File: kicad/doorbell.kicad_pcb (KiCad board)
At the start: 4 copper layers, 52.7 x 58.2 mm, 67 parts, among them J1 USB-C (USB4105), J2 WF26 (6-way screw), K1 G6K-2F-Y 4.5V, K2 G6K-2F-Y 4.5V, K3 G6K-2F-Y 4.5V, Q1 2N7002, Q2 2N7002, Q3 2N7002, SW1 BOOT, SW2 EN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

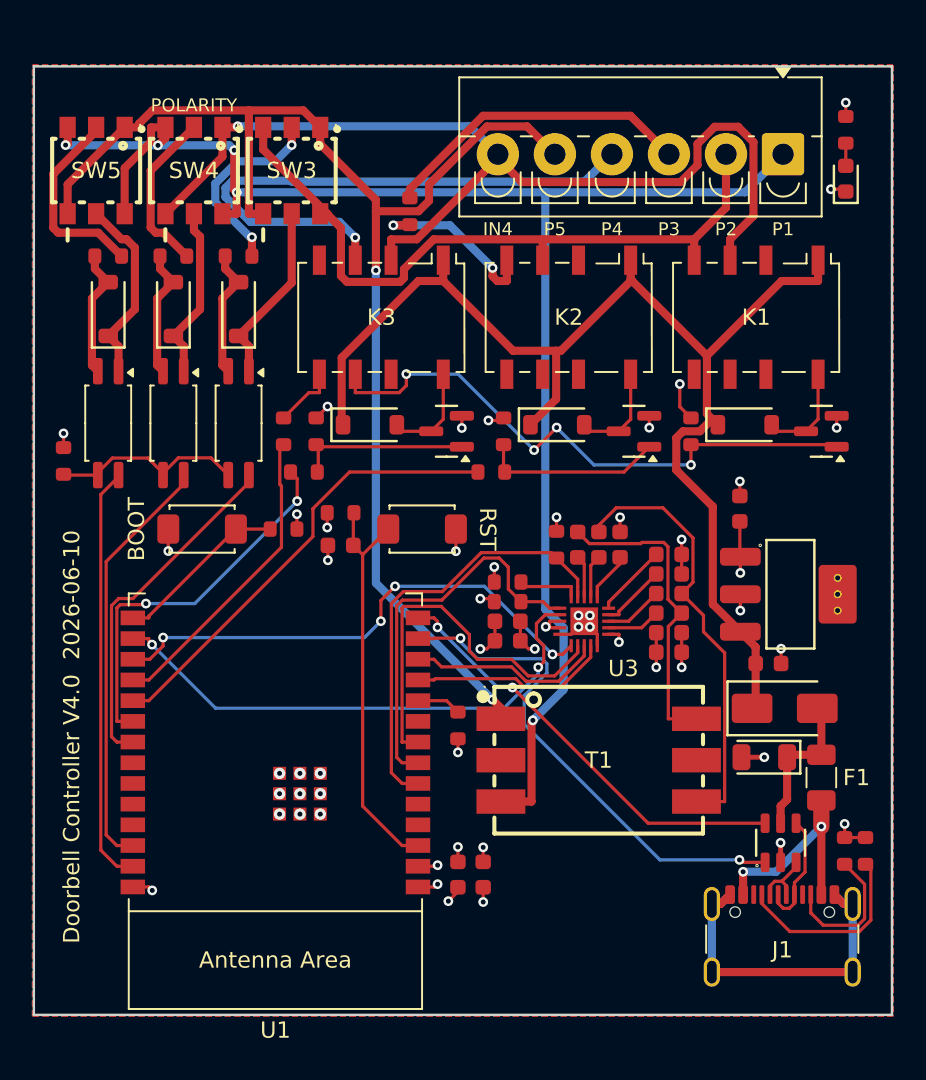
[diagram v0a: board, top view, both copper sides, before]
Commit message: Hand-route GPIO escape bundle; swap GATE pins for crossing-free fan-out
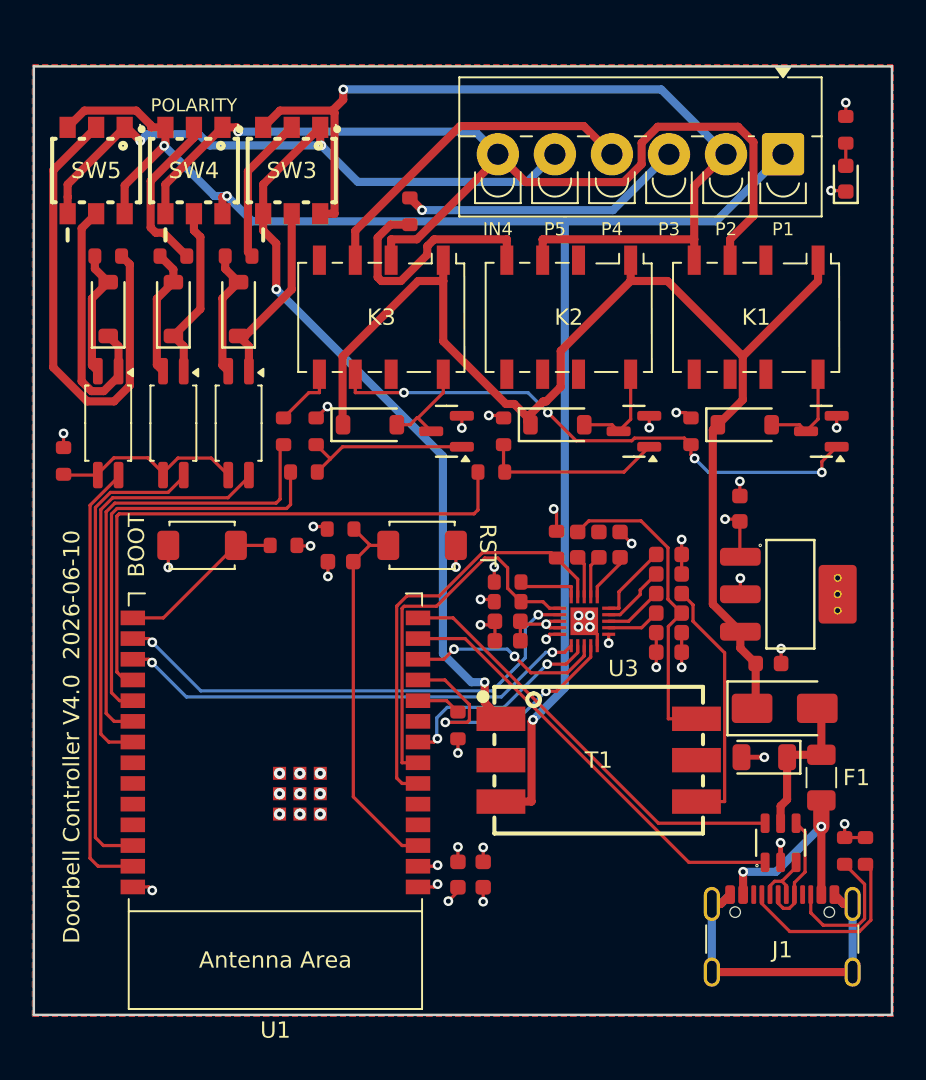
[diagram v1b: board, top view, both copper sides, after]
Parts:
- moved C5 1.00 mm to (17.0, 42.0)
- moved R10 1.00 mm to (17.0, 40.0)
- moved R11 1.00 mm to (13.5, 41.0)
- moved SW1 1.00 mm to (8.50, 41.0)
- moved SW2 1.00 mm to (22.0, 41.0)
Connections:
- U1 pad 18: GATE1_DRV -> GATE2_DRV
- U1 pad 19: GATE2_DRV -> GATE3_DRV
- U1 pad 20: GATE3_DRV -> GATE1_DRV
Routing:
- net OC3_RET: track 12.2 -> 29.9 mm
- net P4: track 35.6 -> 20.9 mm, vias 1 -> 0
- net P2: track 43.4 -> 56.5 mm, vias 0 -> 1
- net SEC_B: track 26.7 -> 15.6 mm
- net I2S_DIN: track 23.4 -> 13.3 mm, vias 0 -> 2
- net GATE1_DRV: track 18.9 -> 28.6 mm
- net GATE2_DRV: track 28.0 -> 35.4 mm
- net I2S_DOUT: track 12.3 -> 17.5 mm, vias 0 -> 2
- net P1: track 99.7 -> 94.5 mm, vias 5 -> 3
- net OC3_JP: track 11.8 -> 16.3 mm
- net OC1_OUT: track 21.5 -> 26.0 mm
- net OT_BRIDGE: track 11.0 -> 15.4 mm, vias 2 -> 0
- net USB_DM_ESP: track 31.3 -> 27.0 mm, vias 2 -> 0
- net OC2_OUT: track 26.0 -> 29.1 mm
- net OC1_RET: track 12.2 -> 9.12 mm, vias 2 -> 0
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
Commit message: Hand-route audio/I2S/USB/bus SE quadrant; fix Freerouting NPE (patched jar in tools/)
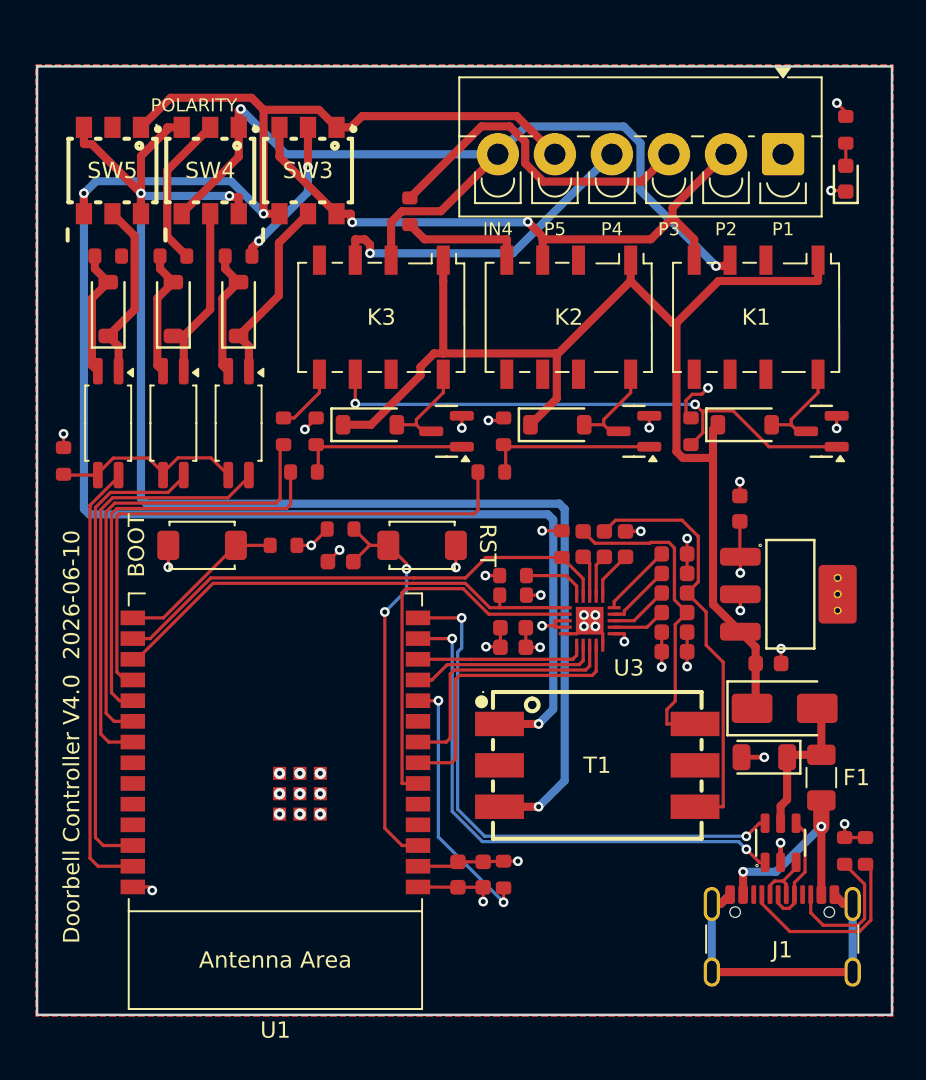
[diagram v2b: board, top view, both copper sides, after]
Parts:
- moved R12 9.57 mm to (27.0, 61.2), turned to 90 degrees
- moved SW3 1.00 mm to (15.0, 18.0)
- moved SW4 1.00 mm to (9.00, 18.0)
- moved SW5 1.00 mm to (3.00, 18.0)
- moved R19 0.52 mm to (27.6, 44.1), turned to 180 degrees
- moved C7 0.52 mm to (27.6, 47.3)
- moved C8 0.52 mm to (27.6, 46.1)
- moved R20 0.52 mm to (27.6, 42.9)
- moved C11 0.34 mm to (37.5, 42.7)
- moved C10 0.34 mm to (37.5, 46.3)
- moved C12 0.34 mm to (34.5, 40.9)
- moved C13 0.34 mm to (37.5, 41.5)
- moved C14 0.34 mm to (37.5, 45.1)
- moved C15 0.34 mm to (37.5, 43.9)
- moved C16 0.34 mm to (31.9, 40.9)
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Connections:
- U1 pad 11: I2S_DOUT -> I2S_DIN
- U1 pad 12: I2S_WS -> I2S_BCLK
- U1 pad 16: I2S_MCLK -> I2C_SDA
- U1 pad 17: I2S_BCLK -> I2C_SCL
- U1 pad 6: I2C_SDA -> I2S_MCLK
- U1 pad 7: I2C_SCL -> I2S_DOUT
- U1 pad 8: I2S_DIN -> I2S_WS
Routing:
- net P5: track 81.0 -> 112.7 mm, vias 4 -> 3
- net OC3_RET: track 29.9 -> 0.00 mm
- net I2S_BCLK: track 29.2 -> 10.5 mm, vias 2 -> 0
- net P2: track 56.5 -> 38.6 mm, vias 1 -> 2
- net GPIO8: track 2.74 -> 16.2 mm, vias 0 -> 2
- net SEC_B: track 15.6 -> 26.0 mm
- net P1: track 94.5 -> 86.1 mm
- net USB_DP_ESP: track 26.5 -> 34.4 mm, vias 0 -> 2
- net OT_BRIDGE: track 15.4 -> 7.60 mm
- net I2S_MCLK: track 30.6 -> 23.5 mm, vias 2 -> 0
- net I2C_SCL: track 23.4 -> 29.9 mm
- net USB_DM_ESP: track 27.0 -> 33.2 mm, vias 0 -> 2
- net IN_P4: track 61.4 -> 55.8 mm, vias 1 -> 2
- net OC3_JP: track 16.3 -> 11.2 mm
- net I2C_SDA: track 26.2 -> 31.3 mm
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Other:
- board size 52.7 x 58.2 mm -> 52.5 x 58.2 mm

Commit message: Move polarity/J2/LED blocks up 2mm; relocate R16; steal OC_CATH/EMIT routes; straighten BCLK
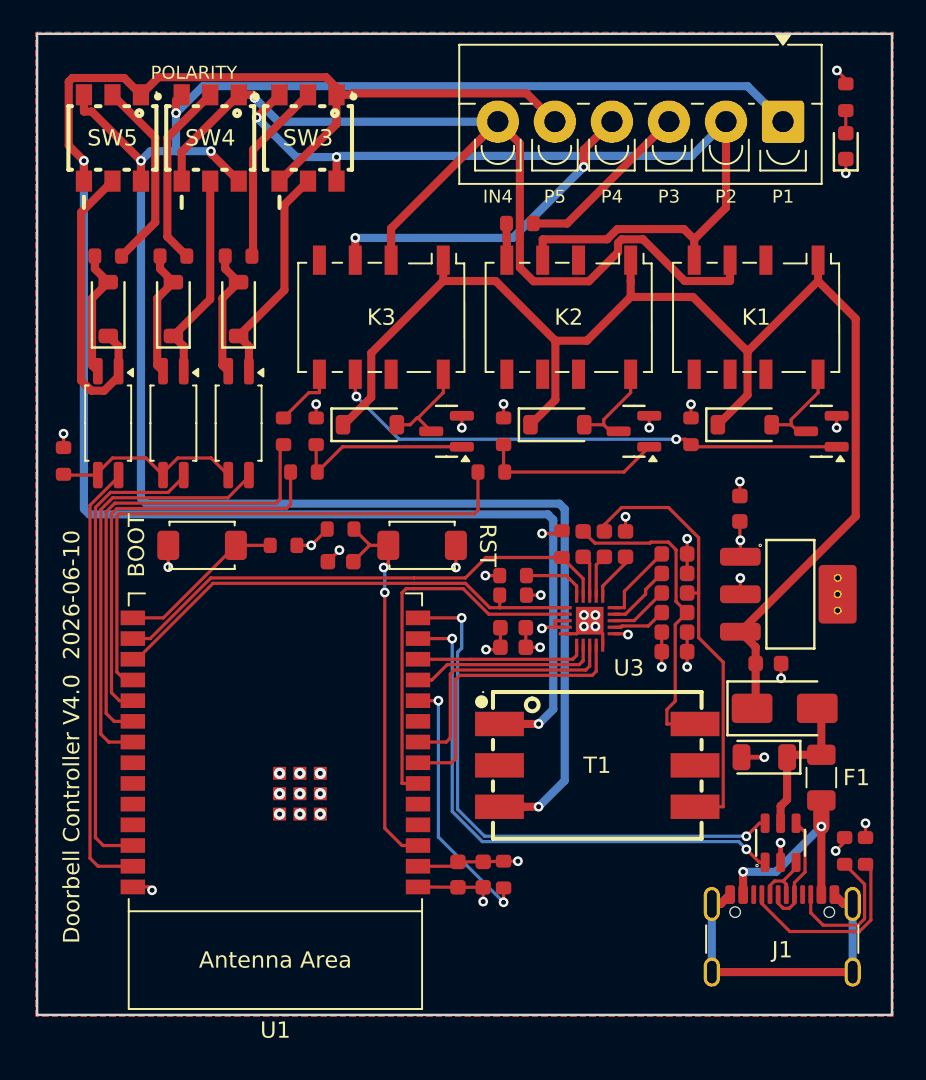
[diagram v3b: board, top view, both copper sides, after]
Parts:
- moved R16 6.79 mm to (28.0, 21.2), turned to 180 degrees
- moved D6 2.00 mm to (48.0, 16.5)
- moved J2 2.00 mm to (44.1, 15.0)
- moved R15 2.00 mm to (48.0, 13.5)
- moved SW3 2.00 mm to (15.0, 16.0)
- moved SW4 2.00 mm to (9.00, 16.0)
- moved SW5 2.00 mm to (3.00, 16.0)
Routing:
- net P1: track 86.1 -> 124.9 mm, vias 3 -> 4
- net P2: track 38.6 -> 54.6 mm
- net OC3_RET: track 0.00 -> 11.8 mm
- net P3: track 20.6 -> 10.9 mm
- net +5V: track 77.5 -> 86.7 mm
- net OC3_JP: track 11.2 -> 18.7 mm
- net OT_BRIDGE: track 7.60 -> 2.26 mm
- net IN_P4: track 55.8 -> 61.1 mm, vias 2 -> 1
- net GND: track 61.3 -> 57.7 mm, vias 36 -> 37
- net GATE1: track 34.8 -> 32.1 mm
- net OC1_RET: track 9.32 -> 11.3 mm, vias 2 -> 0
- net OC1_JP: track 11.7 -> 13.7 mm
- net OC2_RET: track 9.49 -> 11.5 mm
- net OC2_JP: track 11.0 -> 12.9 mm
- net P5: track 112.7 -> 111.4 mm, vias 3 -> 2
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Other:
- board size 52.5 x 58.2 mm -> 52.5 x 60.2 mm

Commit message: Move R6 gate-side of the K3 interlock (K2-style cluster); harden Freerouting patch (4 guard sites)
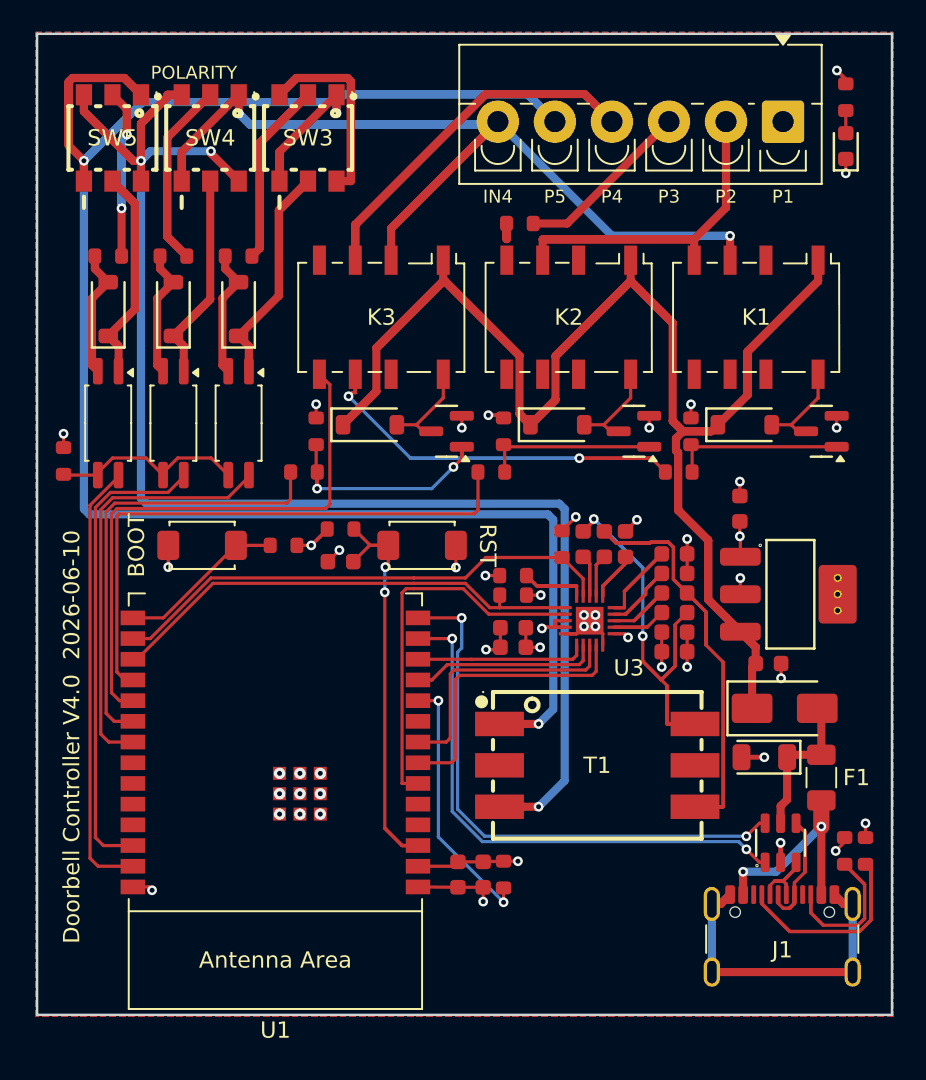
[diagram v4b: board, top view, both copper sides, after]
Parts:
- moved R6 24.4 mm to (37.8, 36.5), turned to 0 degrees
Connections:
- K3 pad 5: GATE1_PRE -> GATE1_DRV
- K3 pad 6: GATE1 -> GATE1_PRE
- R6 pad 1: GATE1_DRV -> GATE1_PRE
- R6 pad 2: GATE1_PRE -> GATE1
- U1 pad 19: GATE3_DRV -> GATE1_DRV
- U1 pad 20: GATE1_DRV -> GATE3_DRV
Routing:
- net +5V: track 86.7 -> 137.6 mm
- net P5: track 111.4 -> 150.4 mm, vias 2 -> 3
- net GATE1_PRE: track 3.97 -> 39.2 mm, vias 0 -> 2
- net IN_P4: track 61.1 -> 88.3 mm, vias 1 -> 2
- net P1: track 124.9 -> 99.8 mm, vias 4 -> 3
- net SEC_B: track 27.0 -> 49.4 mm
- net GATE1: track 32.1 -> 10.7 mm, vias 2 -> 0
- net SEC_A: track 19.4 -> 36.6 mm, vias 0 -> 2
- net P4: track 20.7 -> 37.9 mm, vias 2 -> 0
- net OC1_RET: track 11.3 -> 26.2 mm
- net USB_CC1: track 11.8 -> 23.1 mm
- net OC1_JP: track 13.7 -> 23.0 mm
- net OC2_RET: track 11.5 -> 19.2 mm
- net USB_CC2: track 8.75 -> 15.4 mm
- net USB_DP: track 7.20 -> 13.5 mm
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
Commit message: Reroute P1/P5 bus: T1 around J2 on B.Cu, land pins from the top; swap T1 pins 1/3
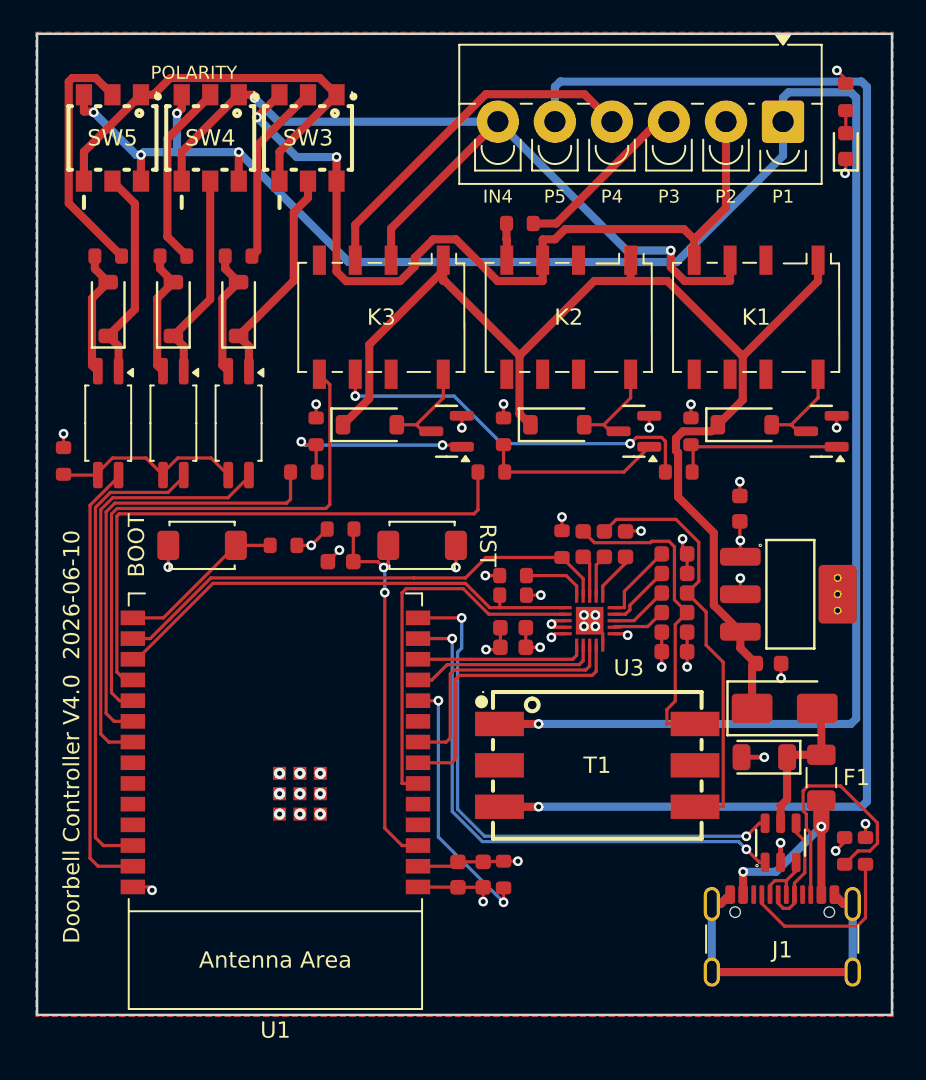
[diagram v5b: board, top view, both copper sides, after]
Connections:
- T1 pad 1: P5 -> P1
- T1 pad 3: P1 -> P5
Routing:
- net +5V: track 137.6 -> 77.4 mm
- net P5: track 150.4 -> 114.5 mm, vias 3 -> 1
- net IN_P4: track 88.3 -> 54.8 mm
- net P1: track 99.8 -> 126.1 mm, vias 3 -> 5
- net SEC_B: track 49.4 -> 25.9 mm
- net SEC_A: track 36.6 -> 19.5 mm, vias 2 -> 0
- net P4: track 37.9 -> 21.9 mm
- net GATE1_PRE: track 39.2 -> 23.7 mm
- net OC1_RET: track 26.2 -> 11.3 mm
- net USB_CC1: track 23.1 -> 11.0 mm
- net OC3_JP: track 22.5 -> 13.2 mm
- net OC1_JP: track 23.0 -> 13.7 mm
- net OC2_RET: track 19.2 -> 11.5 mm
- net USB_DP: track 13.5 -> 7.19 mm
- net P2: track 57.4 -> 51.9 mm, vias 0 -> 2
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
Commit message: Hand-route Px and IN-P4
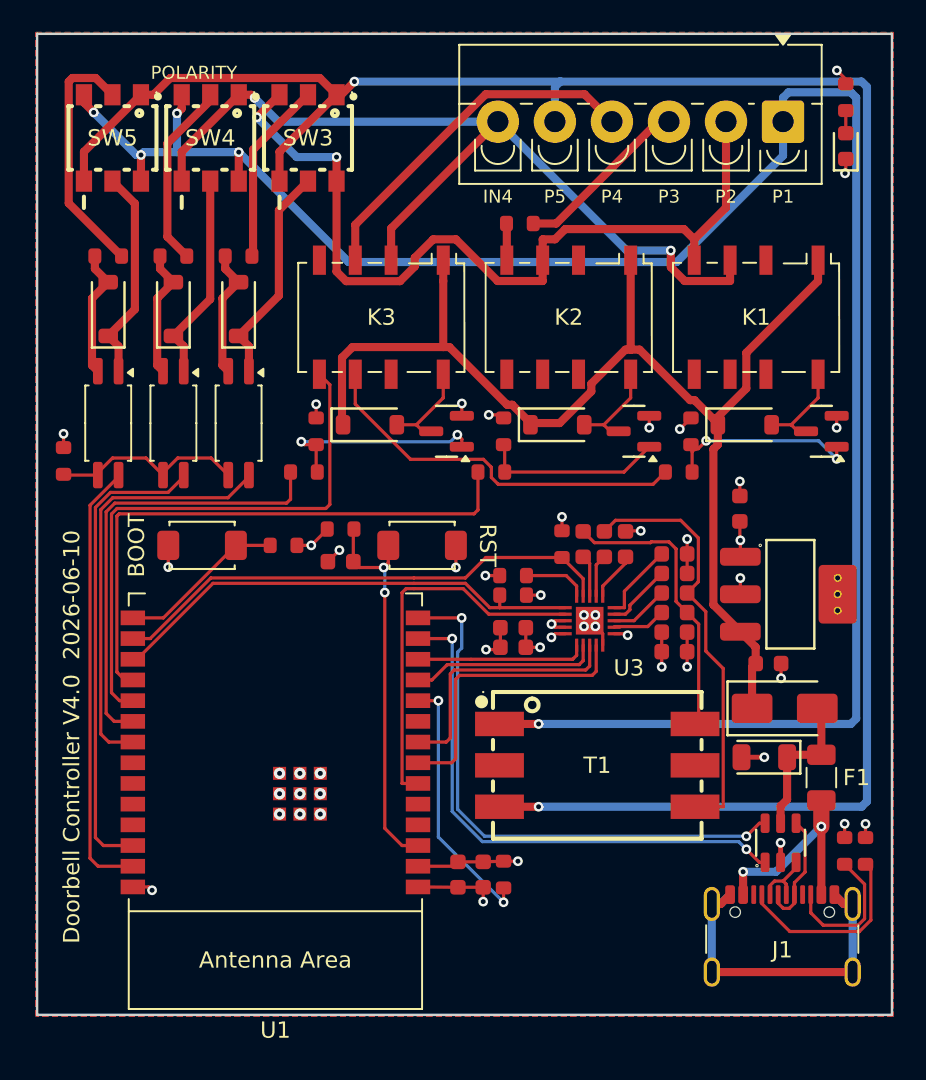
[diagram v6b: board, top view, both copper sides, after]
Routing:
- net P5: track 114.5 -> 128.5 mm, vias 1 -> 2
- net USB_CC2: track 16.0 -> 8.75 mm
- net SEC_A: track 19.5 -> 17.6 mm
- net +5V: track 77.4 -> 75.6 mm
- net GATE1: track 10.6 -> 12.0 mm, vias 0 -> 2
- net USB_CC1: track 11.0 -> 11.8 mm
- net GATE3: track 12.7 -> 13.3 mm
- net GATE1_PRE: track 23.7 -> 23.6 mm, vias 2 -> 0

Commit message: Hand-route U3
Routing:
- net USB_CC2: track 8.75 -> 15.8 mm
- net +3V3: track 20.2 -> 24.1 mm, vias 11 -> 10
- net SEC_A: track 17.6 -> 19.5 mm
- net +5V: track 75.6 -> 77.0 mm
- net GATE1: track 12.0 -> 10.6 mm, vias 2 -> 0
- net USB_CC1: track 11.8 -> 11.0 mm
- net GATE2: track 11.2 -> 10.6 mm
- net GATE1_PRE: track 23.6 -> 23.1 mm, vias 0 -> 2
